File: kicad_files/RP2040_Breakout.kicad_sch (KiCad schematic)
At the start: 0 parts

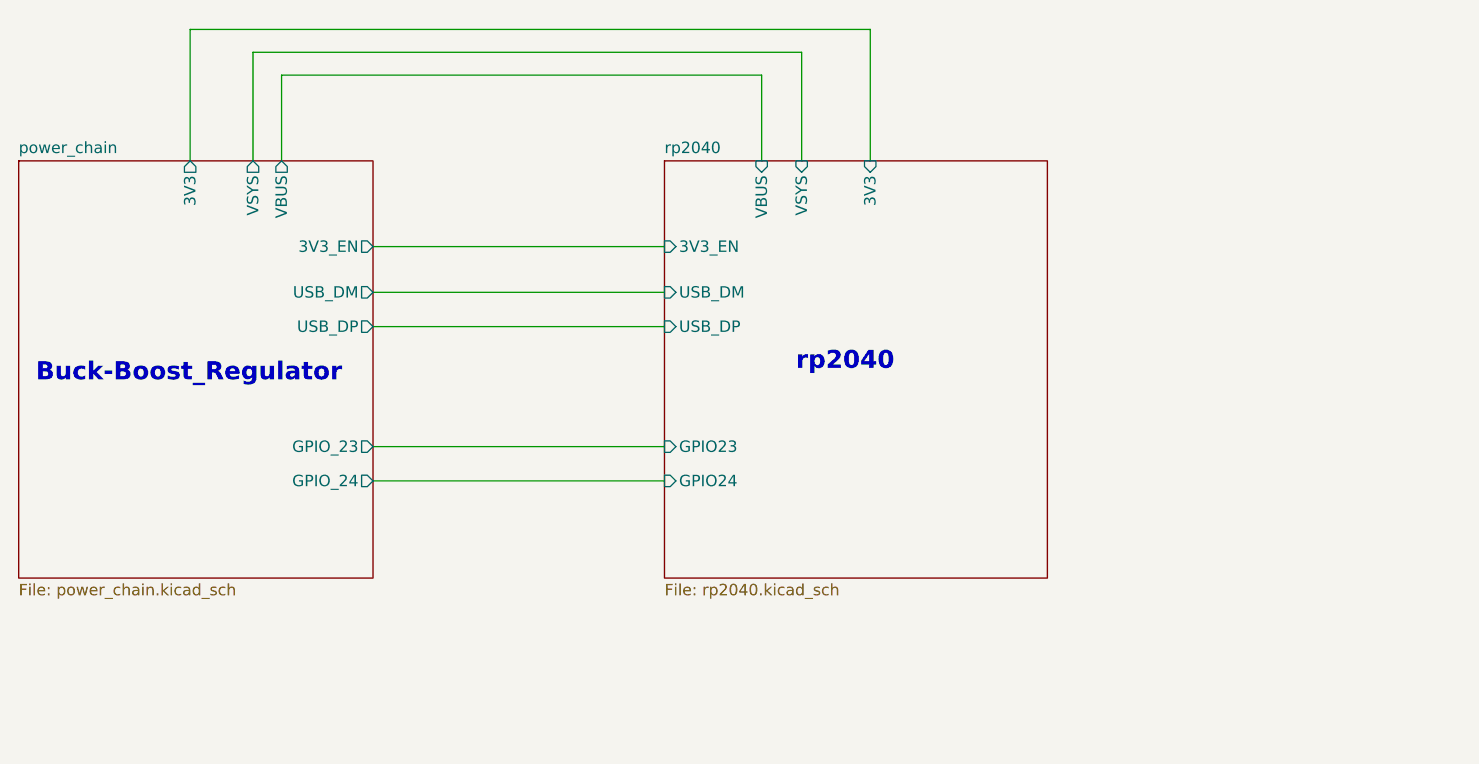
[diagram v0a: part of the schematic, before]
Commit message: back side screen updated
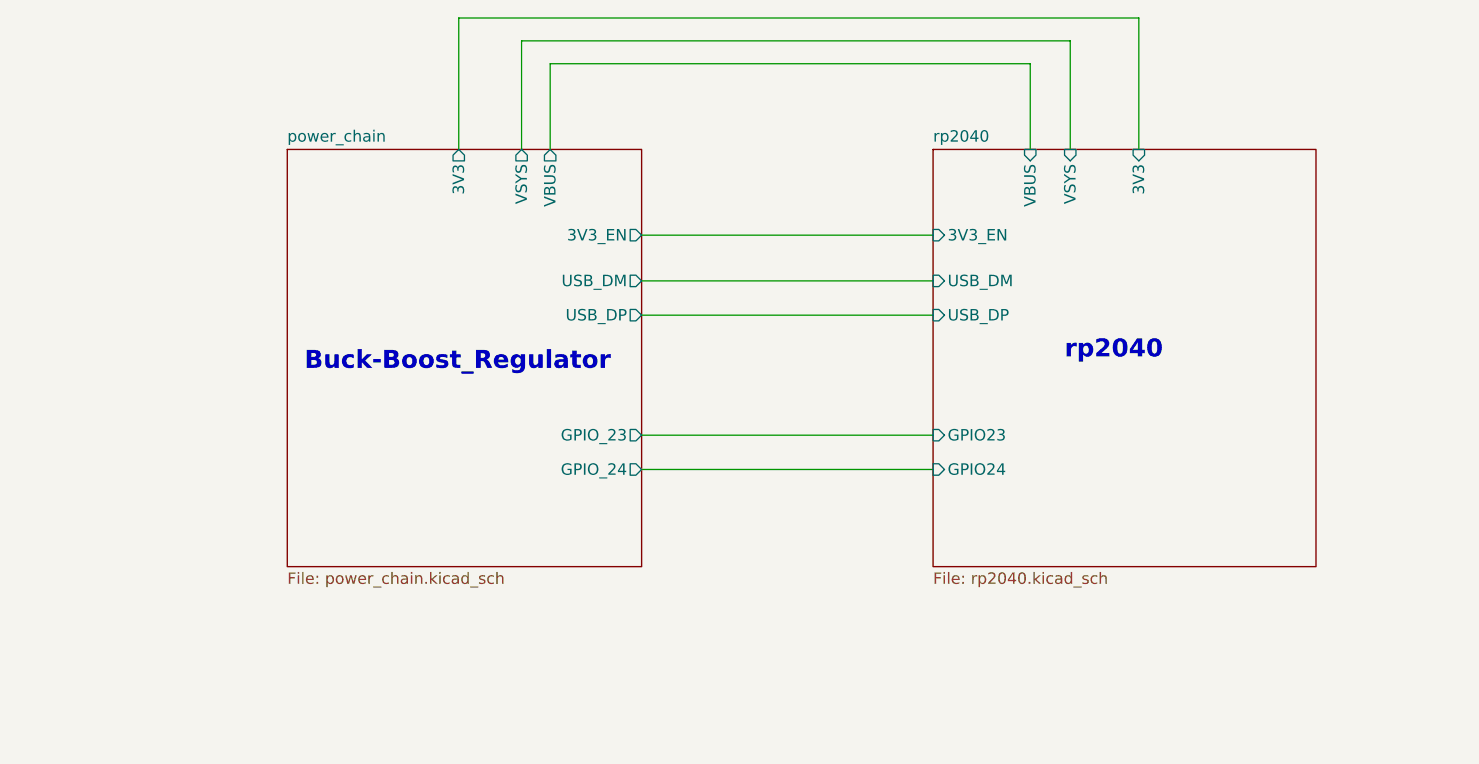
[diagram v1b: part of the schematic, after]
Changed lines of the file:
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@@
     (stroke (width 0) (type default))
   )
-  (wire (pts (xy 133.35 64.77) (xy 133.35 76.835))
+  (wire (pts (xy 163.195 63.5) (xy 163.195 75.565))
     (stroke (width 0) (type default))
   )
-  (wire (pts (xy 85.725 112.395) (xy 118.11 112.395))
+  (wire (pts (xy 115.57 111.125) (xy 147.955 111.125))
     (stroke (width 0) (type default))
   )
-  (wire (pts (xy 140.97 76.835) (xy 140.97 62.23))
+  (wire (pts (xy 170.815 75.565) (xy 170.815 60.96))
     (stroke (width 0) (type default))
   )
-  (wire (pts (xy 85.725 108.585) (xy 118.11 108.585))
+  (wire (pts (xy 115.57 107.315) (xy 147.955 107.315))
     (stroke (width 0) (type default))
   )
-  (wire (pts (xy 140.97 62.23) (xy 65.405 62.23))
+  (wire (pts (xy 170.815 60.96) (xy 95.25 60.96))
     (stroke (width 0) (type default))
   )
-  (wire (pts (xy 75.565 67.31) (xy 128.905 67.31))
+  (wire (pts (xy 105.41 66.04) (xy 158.75 66.04))
     (stroke (width 0) (type default))
   )
-  (wire (pts (xy 72.39 76.835) (xy 72.39 64.77))
+  (wire (pts (xy 102.235 75.565) (xy 102.235 63.5))
     (stroke (width 0) (type default))
   )
-  (wire (pts (xy 75.565 76.835) (xy 75.565 67.31))
+  (wire (pts (xy 105.41 75.565) (xy 105.41 66.04))
     (stroke (width 0) (type default))
   )
-  (wire (pts (xy 85.725 95.25) (xy 118.11 95.25))
+  (wire (pts (xy 115.57 93.98) (xy 147.955 93.98))
     (stroke (width 0) (type default))
   )
-  (wire (pts (xy 72.39 64.77) (xy 133.35 64.77))
+  (wire (pts (xy 102.235 63.5) (xy 163.195 63.5))
     (stroke (width 0) (type default))
   )
-  (wire (pts (xy 128.905 67.31) (xy 128.905 76.835))
+  (wire (pts (xy 158.75 66.04) (xy 158.75 75.565))
     (stroke (width 0) (type default))
   )
-  (wire (pts (xy 65.405 62.23) (xy 65.405 76.835))
+  (wire (pts (xy 95.25 60.96) (xy 95.25 75.565))
     (stroke (width 0) (type default))
   )
-  (wire (pts (xy 85.725 86.36) (xy 118.11 86.36))
+  (wire (pts (xy 115.57 85.09) (xy 147.955 85.09))
     (stroke (width 0) (type default))
   )
-  (wire (pts (xy 85.725 91.44) (xy 118.11 91.44))
+  (wire (pts (xy 115.57 90.17) (xy 147.955 90.17))
     (stroke (width 0) (type default))
   )
-  (text "Buck-Boost_Regulator\n" (at 48.26 101.6 0)
+  (text "Buck-Boost_Regulator\n" (at 78.105 100.33 0)
     (effects (font (size 2 2) (thickness 0.4) bold) (justify left bottom))
   )
-  (text "rp2040\n" (at 132.715 100.33 0)
+  (text "rp2040\n" (at 162.56 99.06 0)
     (effects (font (size 2 2) (thickness 0.4) bold) (justify left bottom))
   )
-  (sheet (at 118.11 76.835) (size 42.545 46.355) (fields_autoplaced)
+  (sheet (at 147.955 75.565) (size 42.545 46.355) (fields_autoplaced)
     (stroke (width 0.1524) (type solid))
     (fill (color 0 0 0 0.0000))
-    (property "Sheetname" "rp2040" (at 118.11 76.1234 0)
+    (property "Sheetname" "rp2040" (at 147.955 74.8534 0)
       (effects (font (size 1.27 1.27)) (justify left bottom))
     )
-    (property "Sheetfile" "rp2040.kicad_sch" (at 118.11 123.7746 0)
+    (property "Sheetfile" "rp2040.kicad_sch" (at 147.955 122.5046 0)
       (effects (font (size 1.27 1.27)) (justify left top))
     )
-    (pin "3V3_EN" input (at 118.11 86.36 180)
+    (pin "3V3_EN" input (at 147.955 85.09 180)
       (effects (font (size 1.27 1.27)) (justify left))
     )
-    (pin "VBUS" input (at 128.905 76.835 90)
+    (pin "VBUS" input (at 158.75 75.565 90)
       (effects (font (size 1.27 1.27)) (justify right))
     )
-    (pin "VSYS" input (at 133.35 76.835 90)
+    (pin "VSYS" input (at 163.195 75.565 90)
       (effects (font (size 1.27 1.27)) (justify right))
     )
-    (pin "USB_DP" input (at 118.11 95.25 180)
+    (pin "USB_DP" input (at 147.955 93.98 180)
       (effects (font (size 1.27 1.27)) (justify left))
     )
-    (pin "USB_DM" input (at 118.11 91.44 180)
+    (pin "USB_DM" input (at 147.955 90.17 180)
       (effects (font (size 1.27 1.27)) (justify left))
     )
-    (pin "GPIO23" input (at 118.11 108.585 180)
+    (pin "GPIO23" input (at 147.955 107.315 180)
       (effects (font (size 1.27 1.27)) (justify left))
     )
-    (pin "GPIO24" input (at 118.11 112.395 180)
+    (pin "GPIO24" input (at 147.955 111.125 180)
       (effects (font (size 1.27 1.27)) (justify left))
     )
-    (pin "3V3" input (at 140.97 76.835 90)
+    (pin "3V3" input (at 170.815 75.565 90)
       (effects (font (size 1.27 1.27)) (justify right))
     )
@@
     )
   )
-  (sheet (at 46.355 76.835) (size 39.37 46.355) (fields_autoplaced)
+  (sheet (at 76.2 75.565) (size 39.37 46.355) (fields_autoplaced)
     (stroke (width 0.1524) (type solid))
     (fill (color 0 0 0 0.0000))
-    (property "Sheetname" "power_chain" (at 46.355 76.1234 0)
+    (property "Sheetname" "power_chain" (at 76.2 74.8534 0)
       (effects (font (size 1.27 1.27)) (justify left bottom))
     )
-    (property "Sheetfile" "power_chain.kicad_sch" (at 46.355 123.7746 0)
+    (property "Sheetfile" "power_chain.kicad_sch" (at 76.2 122.5046 0)
       (effects (font (size 1.27 1.27)) (justify left top))
     )
-    (pin "GPIO_23" output (at 85.725 108.585 0)
+    (pin "GPIO_23" output (at 115.57 107.315 0)
       (effects (font (size 1.27 1.27)) (justify right))
     )
-    (pin "GPIO_24" output (at 85.725 112.395 0)
+    (pin "GPIO_24" output (at 115.57 111.125 0)
       (effects (font (size 1.27 1.27)) (justify right))
     )
-    (pin "USB_DM" output (at 85.725 91.44 0)
+    (pin "USB_DM" output (at 115.57 90.17 0)
       (effects (font (size 1.27 1.27)) (justify right))
     )
-    (pin "USB_DP" output (at 85.725 95.25 0)
+    (pin "USB_DP" output (at 115.57 93.98 0)
       (effects (font (size 1.27 1.27)) (justify right))
     )
-    (pin "3V3_EN" output (at 85.725 86.36 0)
+    (pin "3V3_EN" output (at 115.57 85.09 0)
       (effects (font (size 1.27 1.27)) (justify right))
     )
-    (pin "3V3" output (at 65.405 76.835 90)
+    (pin "3V3" output (at 95.25 75.565 90)
       (effects (font (size 1.27 1.27)) (justify right))
     )
-    (pin "VSYS" output (at 72.39 76.835 90)
+    (pin "VSYS" output (at 102.235 75.565 90)
       (effects (font (size 1.27 1.27)) (justify right))
     )
-    (pin "VBUS" output (at 75.565 76.835 90)
+    (pin "VBUS" output (at 105.41 75.565 90)
       (effects (font (size 1.27 1.27)) (justify right))
     )
